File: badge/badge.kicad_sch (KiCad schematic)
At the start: 59 parts, among them J1 Conn_02x03_Odd_Even, Q1 BSS83P, SW1 SK-3296S-01-L1, SW2 SW_Push, U1 ATtiny424-SSU, U2 MT3608

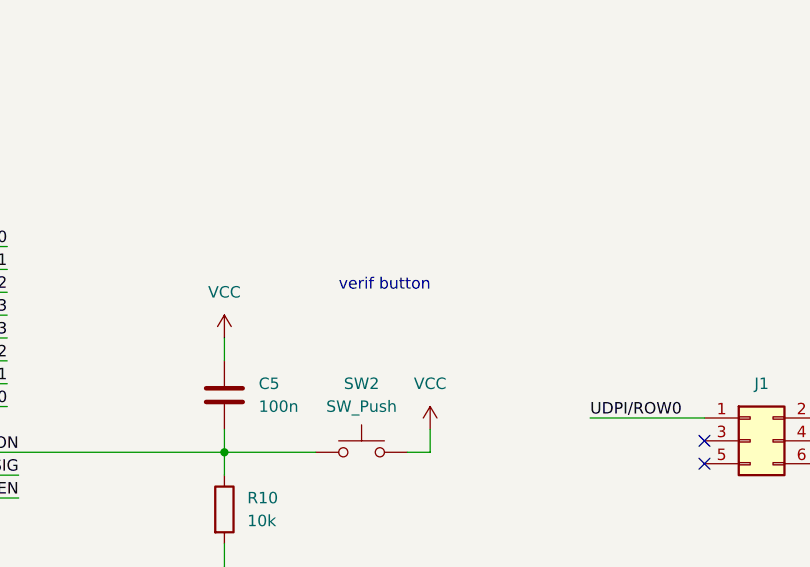
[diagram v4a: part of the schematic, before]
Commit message: updated the footprint of the badge and corrected the button footprint
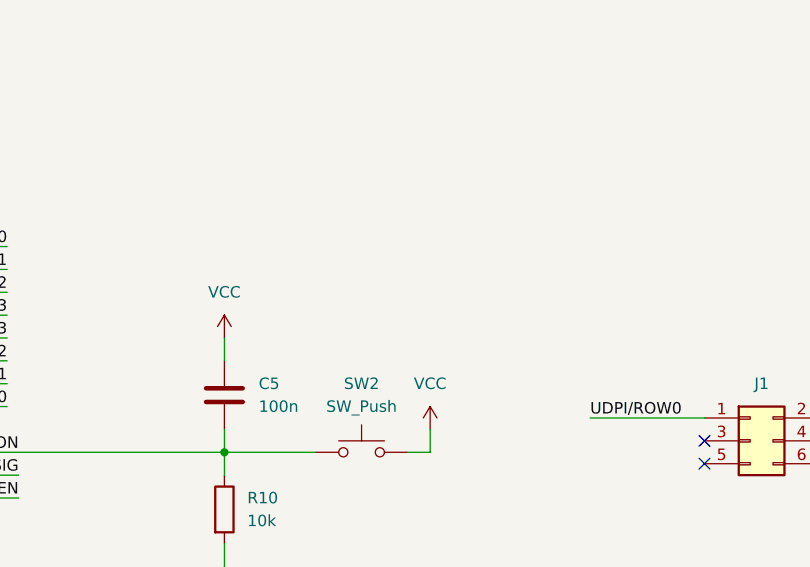
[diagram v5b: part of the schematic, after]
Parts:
- SW2: footprint Button_Switch_SMD:SW_Push_1P1T_NO_CK_KSC6xxJ -> Button_Switch_SMD:SW_Push_1P1T_NO_6x6mm_H9.5mm
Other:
- note removed: "verif button"
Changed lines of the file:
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@@
     (stroke (width 0) (type default) (color 0 0 0 0))
-  )
-  (text "verif button\n" (at 110.49 154.94 0)
-    (effects (font (size 1.27 1.27)) (justify left bottom))
   )
   (label "ROW2" (at 73.66 154.94 180)
@@
     (property "Reference" "SW2" (id 0) (at 113.03 165.1 0))
     (property "Value" "SW_Push" (id 1) (at 113.03 167.64 0))
-    (property "Footprint" "Button_Switch_SMD:SW_Push_1P1T_NO_CK_KSC6xxJ" (id 2) (at 113.03 167.64 0)
+    (property "Footprint" "Button_Switch_SMD:SW_Push_1P1T_NO_6x6mm_H9.5mm" (id 2) (at 113.03 167.64 0)
       (effects (font (size 1.27 1.27)) hide)
     )
@@
     )
     (path "/11f74aa4-46af-431f-9c53-aa9429b4268a"
-      (reference "SW2") (unit 1) (value "SW_Push") (footprint "Button_Switch_SMD:SW_Push_1P1T_NO_CK_KSC6xxJ")
+      (reference "SW2") (unit 1) (value "SW_Push") (footprint "Button_Switch_SMD:SW_Push_1P1T_NO_6x6mm_H9.5mm")
     )
     (path "/94dbc41a-cbcf-45a2-b206-e5a9e1ca811c"
